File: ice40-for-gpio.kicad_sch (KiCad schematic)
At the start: 30 parts, among them U5 ICE40UP5K-SG48ITR, U6 W25Q128JVS, U7 LP5907MFX-1.2

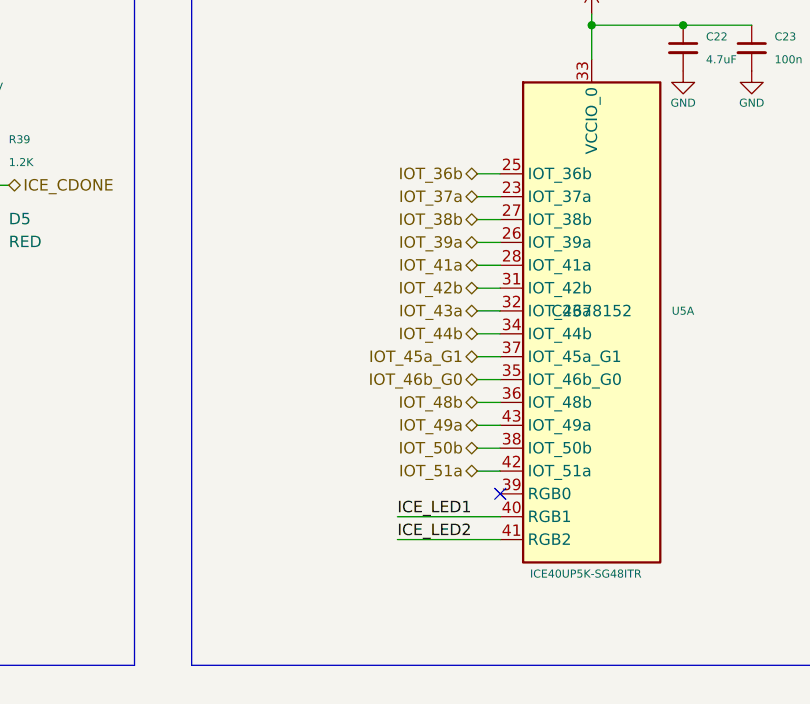
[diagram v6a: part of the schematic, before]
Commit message: Improve the routing
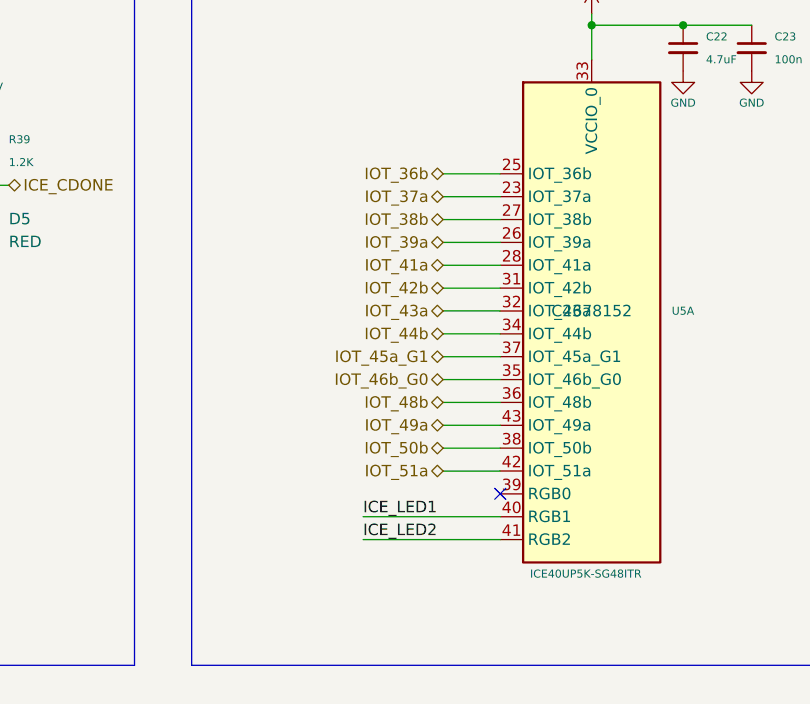
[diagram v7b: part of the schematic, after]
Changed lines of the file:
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@@
 	(wire
 		(pts
-			(xy 146.05 120.65) (xy 148.59 120.65)
+			(xy 142.24 120.65) (xy 148.59 120.65)
 		)
 		(stroke
@@
 	(wire
 		(pts
-			(xy 146.05 130.81) (xy 148.59 130.81)
+			(xy 142.24 130.81) (xy 148.59 130.81)
 		)
 		(stroke
@@
 	(wire
 		(pts
-			(xy 146.05 113.03) (xy 148.59 113.03)
+			(xy 142.24 113.03) (xy 148.59 113.03)
 		)
 		(stroke
@@
 	(wire
 		(pts
-			(xy 146.05 110.49) (xy 148.59 110.49)
+			(xy 142.24 110.49) (xy 148.59 110.49)
 		)
 		(stroke
@@
 	(wire
 		(pts
-			(xy 146.05 123.19) (xy 148.59 123.19)
+			(xy 142.24 123.19) (xy 148.59 123.19)
 		)
 		(stroke
@@
 	(wire
 		(pts
-			(xy 146.05 107.95) (xy 148.59 107.95)
+			(xy 142.24 107.95) (xy 148.59 107.95)
 		)
 		(stroke
@@
 	(wire
 		(pts
-			(xy 146.05 115.57) (xy 148.59 115.57)
+			(xy 142.24 115.57) (xy 148.59 115.57)
 		)
 		(stroke
@@
 	(wire
 		(pts
-			(xy 137.16 140.97) (xy 148.59 140.97)
+			(xy 133.35 140.97) (xy 148.59 140.97)
 		)
 		(stroke
@@
 	(wire
 		(pts
-			(xy 146.05 128.27) (xy 148.59 128.27)
+			(xy 142.24 128.27) (xy 148.59 128.27)
 		)
 		(stroke
@@
 	(wire
 		(pts
-			(xy 146.05 105.41) (xy 148.59 105.41)
-		)
-		(stroke
-			(width 0)
-			(type default)
-		)
-	)
-	(wire
-		(pts
-			(xy 146.05 133.35) (xy 148.59 133.35)
+			(xy 142.24 105.41) (xy 148.59 105.41)
+		)
+		(stroke
+			(width 0)
+			(type default)
+		)
+	)
+	(wire
+		(pts
+			(xy 142.24 133.35) (xy 148.59 133.35)
 		)
 		(stroke
@@
 	(wire
 		(pts
-			(xy 137.16 138.43) (xy 148.59 138.43)
+			(xy 133.35 138.43) (xy 148.59 138.43)
 		)
 		(stroke
@@
 	(wire
 		(pts
-			(xy 146.05 100.33) (xy 148.59 100.33)
+			(xy 142.24 100.33) (xy 148.59 100.33)
 		)
 		(stroke
@@
 	(wire
 		(pts
-			(xy 146.05 118.11) (xy 148.59 118.11)
+			(xy 142.24 118.11) (xy 148.59 118.11)
 		)
 		(stroke
@@
 	(wire
 		(pts
-			(xy 146.05 102.87) (xy 148.59 102.87)
+			(xy 142.24 102.87) (xy 148.59 102.87)
 		)
 		(stroke
@@
 	(wire
 		(pts
-			(xy 146.05 125.73) (xy 148.59 125.73)
+			(xy 142.24 125.73) (xy 148.59 125.73)
 		)
 		(stroke
@@
 	)
 	(label "ICE_LED2"
-		(at 137.16 140.97 0)
+		(at 133.35 140.97 0)
 		(effects
 			(font
@@
 	)
 	(label "ICE_LED1"
-		(at 137.16 138.43 0)
+		(at 133.35 138.43 0)
 		(effects
 			(font
@@
 	(hierarchical_label "IOT_43a"
 		(shape bidirectional)
-		(at 146.05 115.57 180)
+		(at 142.24 115.57 180)
 		(effects
 			(font
@@
 	(hierarchical_label "IOT_51a"
 		(shape bidirectional)
-		(at 146.05 133.35 180)
+		(at 142.24 133.35 180)
 		(effects
 			(font
@@
 	(hierarchical_label "IOT_46b_G0"
 		(shape bidirectional)
-		(at 146.05 123.19 180)
+		(at 142.24 123.19 180)
 		(effects
 			(font
@@
 	(hierarchical_label "IOT_48b"
 		(shape bidirectional)
-		(at 146.05 125.73 180)
+		(at 142.24 125.73 180)
 		(effects
 			(font
@@
 	(hierarchical_label "IOT_49a"
 		(shape bidirectional)
-		(at 146.05 128.27 180)
+		(at 142.24 128.27 180)
 		(effects
 			(font
@@
 	(hierarchical_label "IOT_42b"
 		(shape bidirectional)
-		(at 146.05 113.03 180)
+		(at 142.24 113.03 180)
 		(effects
 			(font
@@
 	(hierarchical_label "IOT_44b"
 		(shape bidirectional)
-		(at 146.05 118.11 180)
+		(at 142.24 118.11 180)
 		(effects
 			(font
@@
 	(hierarchical_label "IOT_39a"
 		(shape bidirectional)
-		(at 146.05 107.95 180)
+		(at 142.24 107.95 180)
 		(effects
 			(font
@@
 	(hierarchical_label "IOT_45a_G1"
 		(shape bidirectional)
-		(at 146.05 120.65 180)
+		(at 142.24 120.65 180)
 		(effects
 			(font
@@
 	(hierarchical_label "IOT_37a"
 		(shape bidirectional)
-		(at 146.05 102.87 180)
+		(at 142.24 102.87 180)
 		(effects
 			(font
@@
 	(hierarchical_label "IOT_36b"
 		(shape bidirectional)
-		(at 146.05 100.33 180)
+		(at 142.24 100.33 180)
 		(effects
 			(font
@@
 	(hierarchical_label "IOT_50b"
 		(shape bidirectional)
-		(at 146.05 130.81 180)
+		(at 142.24 130.81 180)
 		(effects
 			(font
@@
 	(hierarchical_label "IOT_41a"
 		(shape bidirectional)
-		(at 146.05 110.49 180)
+		(at 142.24 110.49 180)
 		(effects
 			(font
@@
 	(hierarchical_label "IOT_38b"
 		(shape bidirectional)
-		(at 146.05 105.41 180)
-		(effects
-			(font
+		(at 142.24 105.41 180)
+		(effects
+			(font
